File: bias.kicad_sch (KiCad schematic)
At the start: 25 parts, among them Q2001 DPLS350E, Q2002 DNLS350E, Q2003 DPLS350E, Q2004 DPLS350E, Q2005 DNLS350E, Q2006 DNLS350E, Q2007 TIP41C, Q2008 TIP42C

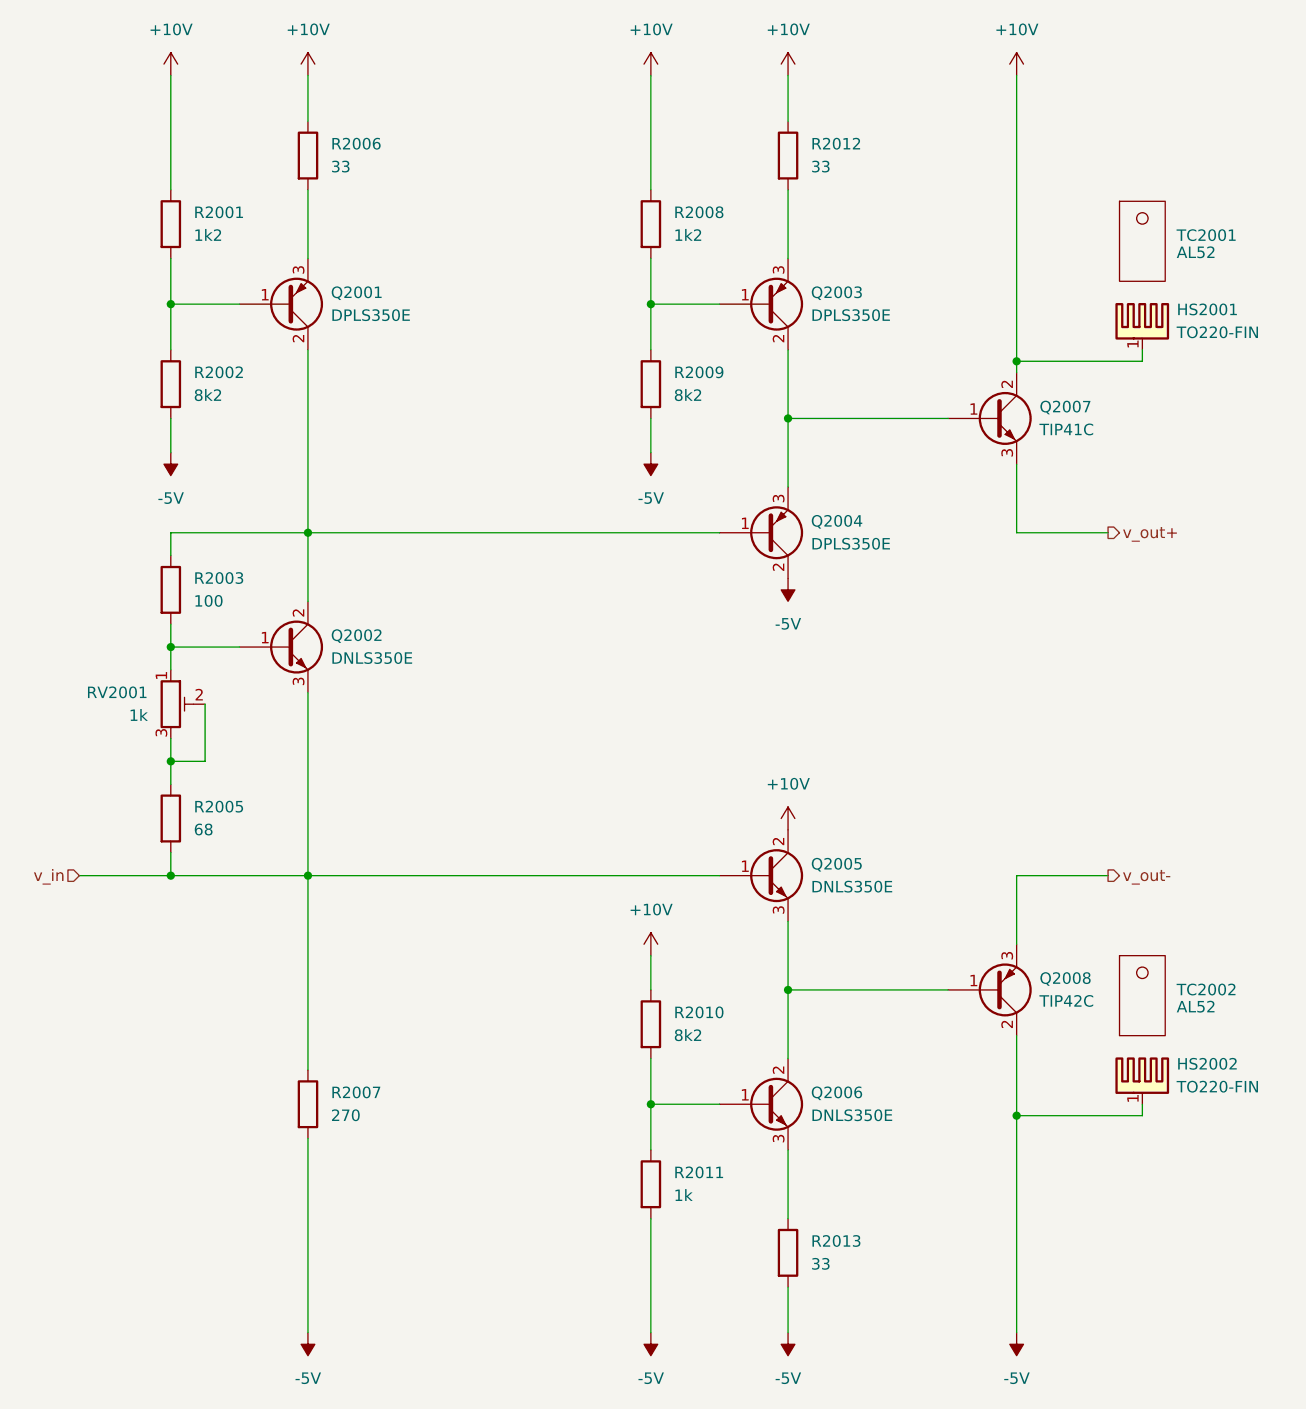
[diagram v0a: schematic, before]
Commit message: add pss 3dmodels and testpoints
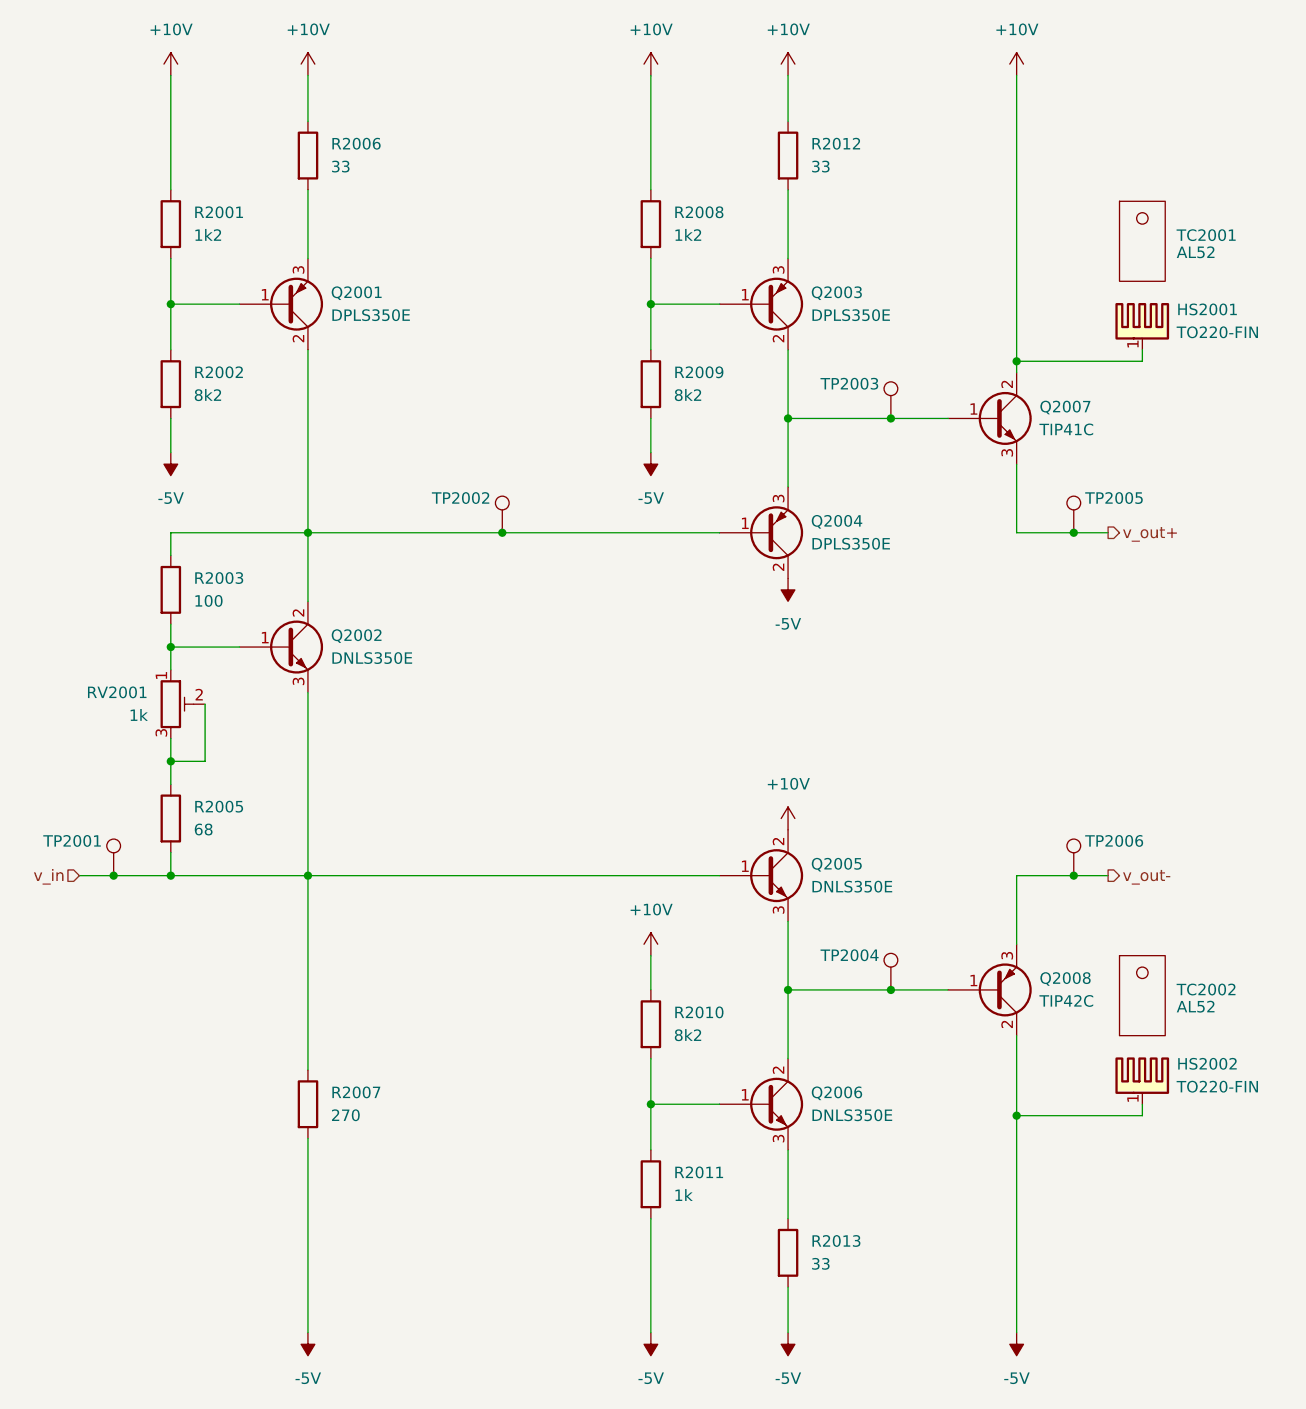
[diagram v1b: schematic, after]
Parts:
- added TP2001, TP2002, TP2003, TP2004, TP2005, TP2006: ~, pss:TP_0805_2012Metric, symbol Connector:TestPoint
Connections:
- net v_in: now also TP2001.1
- net v_out+: now also TP2005.1
- net v_out-: now also TP2006.1
- net at Q2003.2 (C), Q2004.3 (E), Q2007.1 (B): now also TP2003.1
- net at Q2001.2 (C), Q2002.2 (C), Q2004.1 (B)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: now also TP2002.1
- net at Q2005.3 (E), Q2006.2 (C), Q2008.1 (B): now also TP2004.1

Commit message: add bias separate power supply net
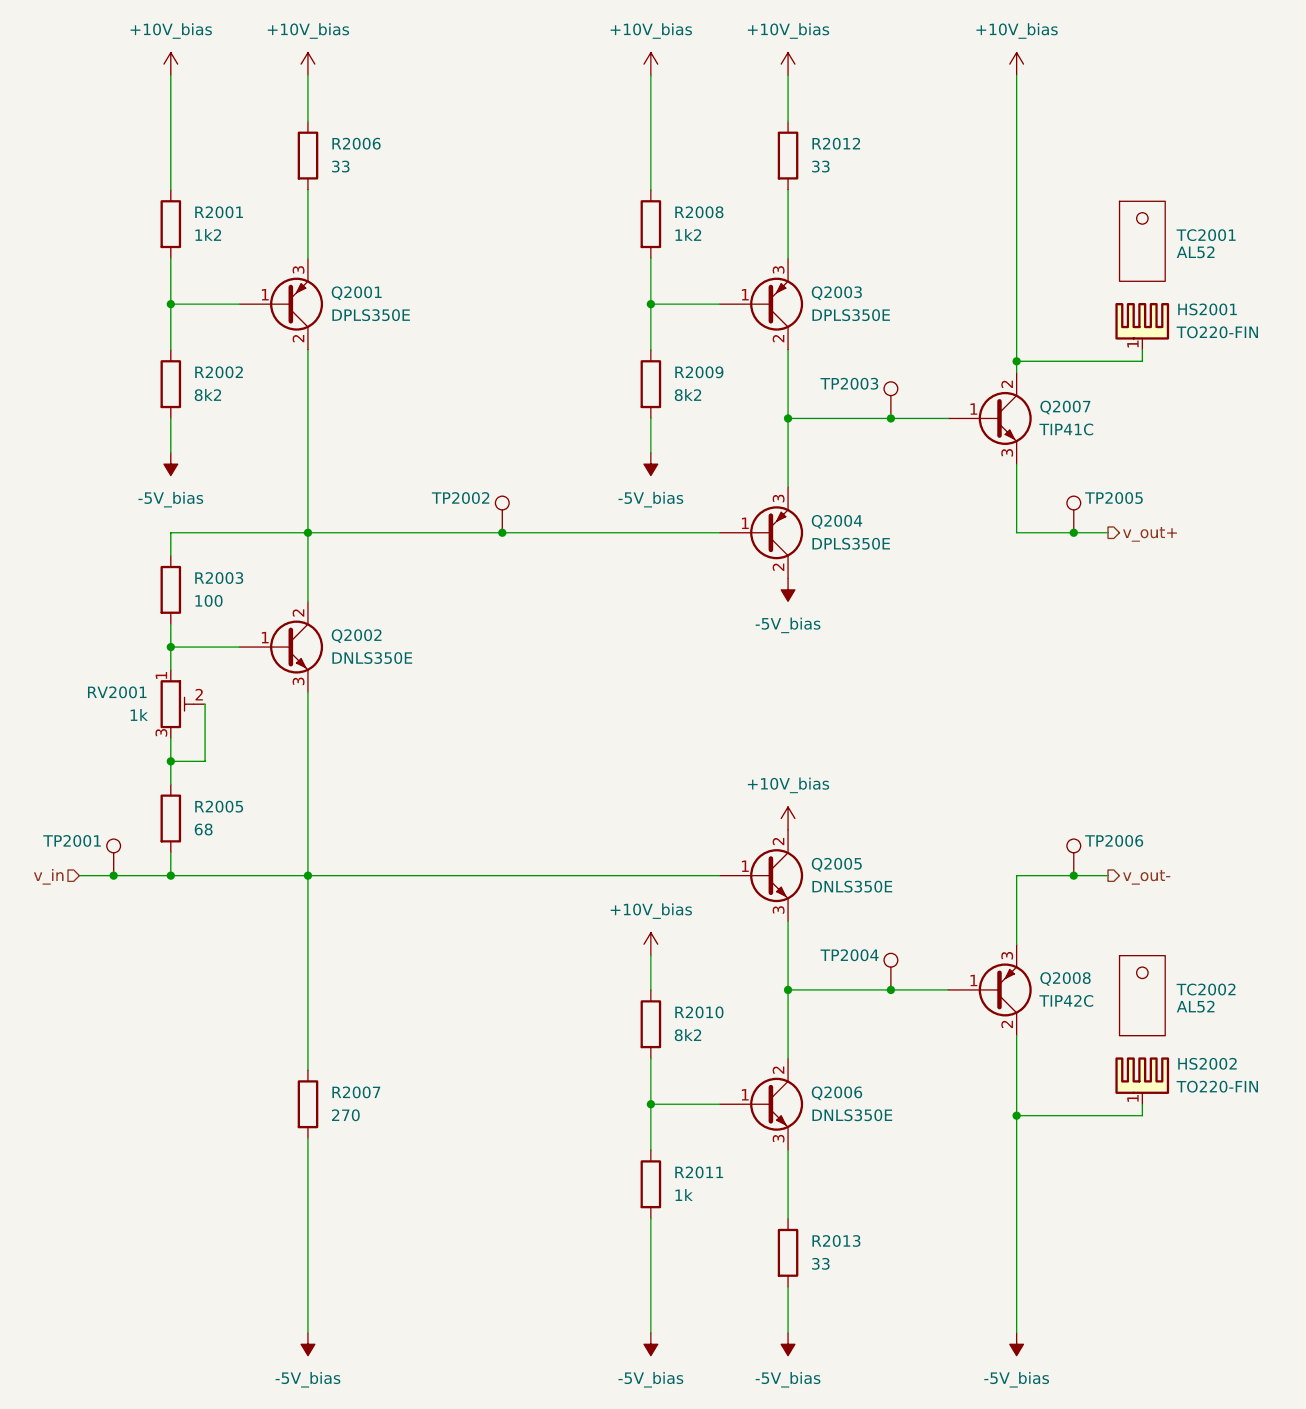
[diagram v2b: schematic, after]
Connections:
- net +10V renamed +10V_bias
- net -5V renamed -5V_bias

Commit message: edit pss symbol library: export all schematic symbols to library 'pss' and update symbol link
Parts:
- RV2001: symbol Device:R_Potentiometer_Trim -> pss:R_Potentiometer_Trim
- TP2001, TP2002, TP2003, TP2004, TP2005, TP2006: symbol Connector:TestPoint -> pss:TestPoint
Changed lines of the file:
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@@
 	)
 	(symbol
-		(lib_id "Connector:TestPoint")
+		(lib_id "pss:TestPoint")
 		(at 140.97 139.7 0)
 		(mirror y)
@@
 	)
 	(symbol
-		(lib_id "Connector:TestPoint")
+		(lib_id "pss:TestPoint")
 		(at 161.29 127 0)
 		(unit 1)
@@
 	)
 	(symbol
-		(lib_id "Connector:TestPoint")
+		(lib_id "pss:TestPoint")
 		(at 161.29 88.9 0)
 		(unit 1)
@@
 	)
 	(symbol
-		(lib_id "Connector:TestPoint")
+		(lib_id "pss:TestPoint")
 		(at 140.97 76.2 0)
 		(mirror y)
@@
 	)
 	(symbol
-		(lib_id "Device:R_Potentiometer_Trim")
+		(lib_id "pss:R_Potentiometer_Trim")
 		(at 60.96 107.95 0)
 		(unit 1)
@@
 	)
 	(symbol
-		(lib_id "Connector:TestPoint")
+		(lib_id "pss:TestPoint")
 		(at 97.79 88.9 0)
 		(mirror y)
@@
 	)
 	(symbol
-		(lib_id "Connector:TestPoint")
+		(lib_id "pss:TestPoint")
 		(at 54.61 127 0)
 		(mirror y)
